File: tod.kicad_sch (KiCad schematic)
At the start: 65 parts, among them J1 2xMVE252, J2 MV133, J3 2xMVE252, J4 MV133, Q1 BC856B, Q2 BC817, Q3 BC856B, Q4 BC817, Q5 BC856B, Q6 BC817, Q7 BC856B, Q8 BC817, U1 PC817, U2 PC817, U3 PC817, U4 PC817

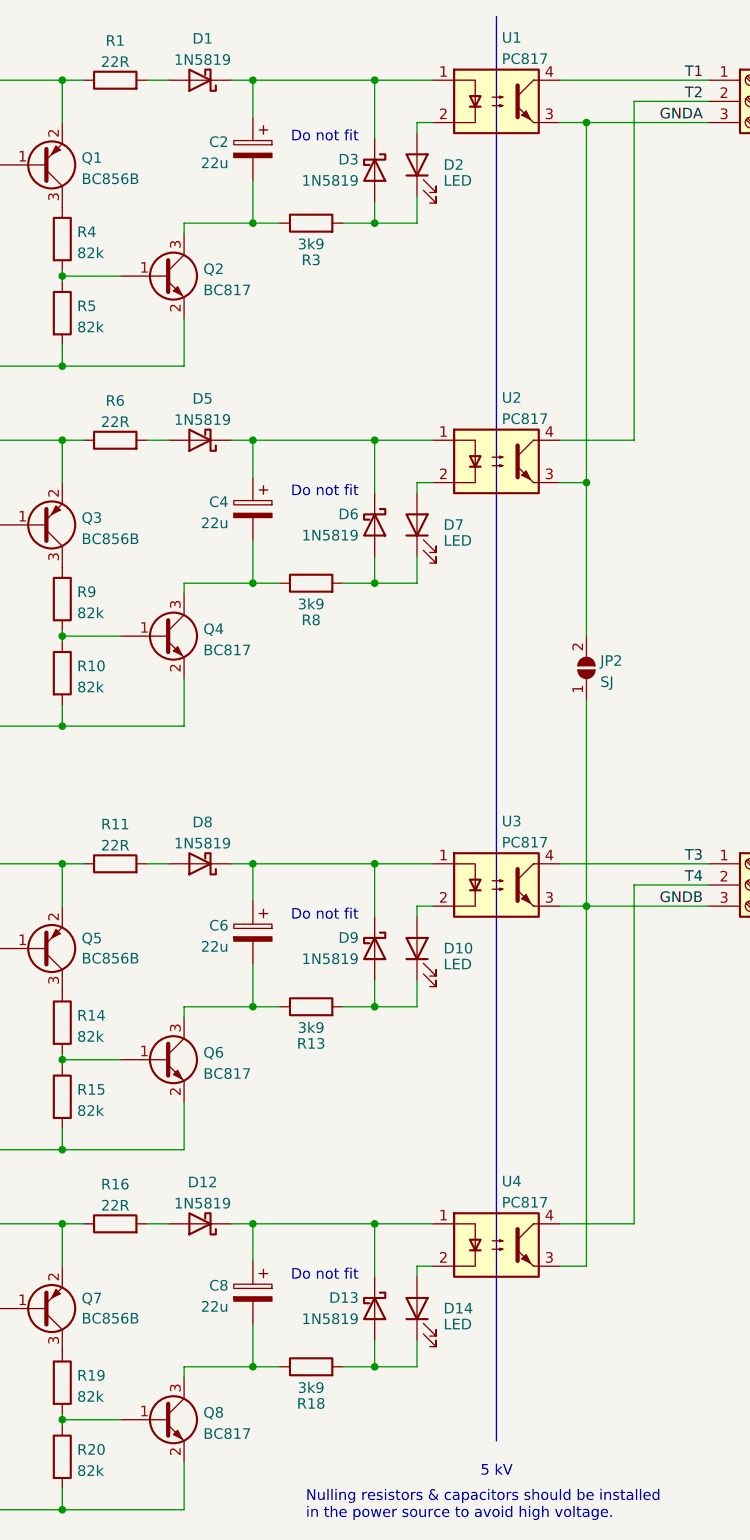
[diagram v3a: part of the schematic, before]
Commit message: Use DNP where appropriate.
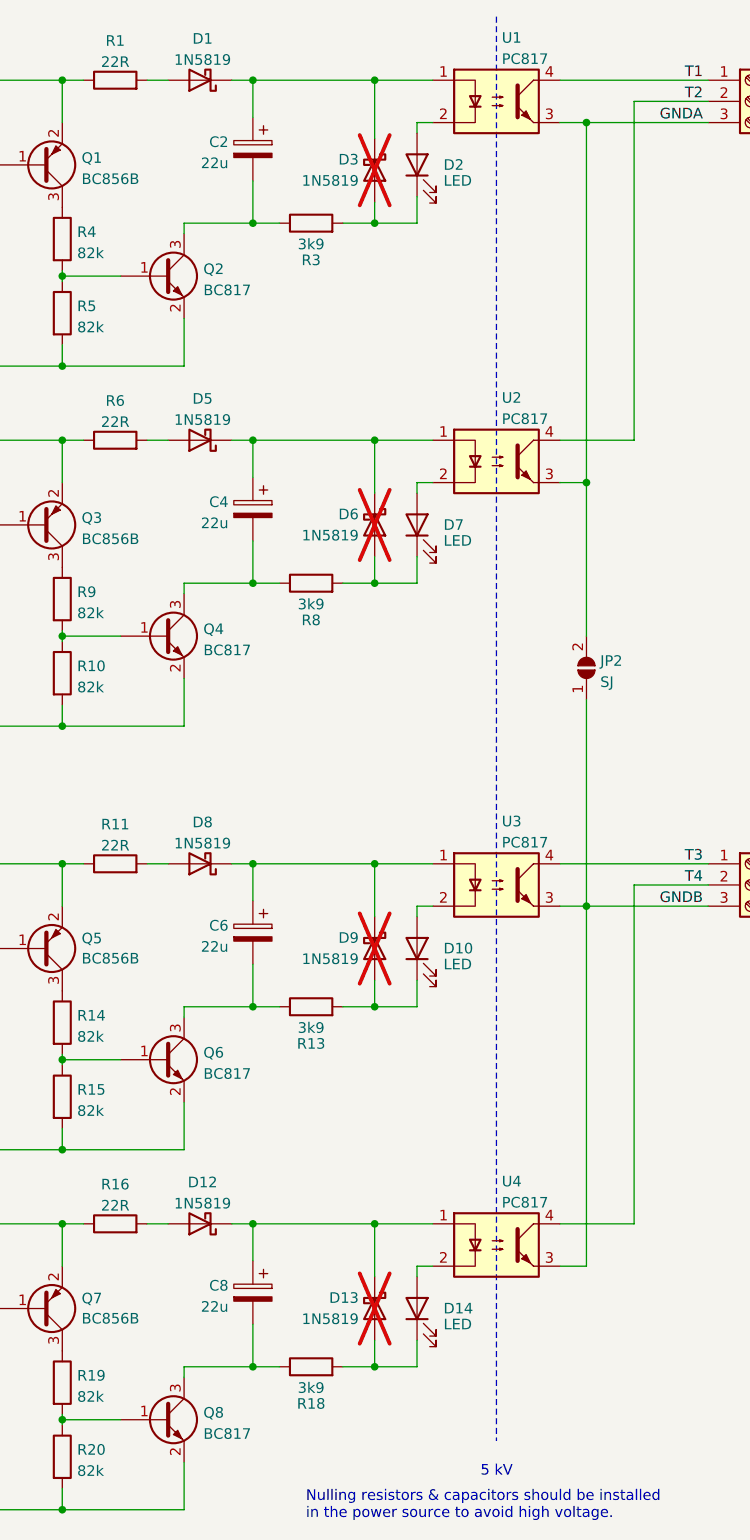
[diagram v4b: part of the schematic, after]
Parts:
- D13, D3, D6, D9: now not fitted
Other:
- note removed: "Do not fit"
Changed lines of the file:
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@@
   )
   (polyline (pts (xy 146.05 13.97) (xy 146.05 184.785))
-    (stroke (width 0) (type default))
+    (stroke (width 0) (type dash))
   )
   (wire (pts (xy 153.67 163.83) (xy 156.845 163.83))
@@
   (wire (pts (xy 131.445 158.75) (xy 138.43 158.75))
     (stroke (width 0) (type default))
-  )
-  (text "Do not fit" (at 129.54 165.735 0)
-    (effects (font (size 1.27 1.27)) (justify right bottom))
-  )
-  (text "Do not fit" (at 129.54 71.755 0)
-    (effects (font (size 1.27 1.27)) (justify right bottom))
   )
   (text "Up to ~2.5 W\nheat loss!" (at 31.242 43.688 0)
@@
     (effects (font (size 1.27 1.27)) (justify left bottom))
   )
-  (text "Do not fit" (at 129.54 122.555 0)
-    (effects (font (size 1.27 1.27)) (justify right bottom))
-  )
-  (text "Do not fit" (at 129.54 29.21 0)
-    (effects (font (size 1.27 1.27)) (justify right bottom))
-  )
   (label "K1" (at 29.21 26.67 0) (fields_autoplaced)
     (effects (font (size 1.27 1.27)) (justify left bottom))
@@
   )
   (symbol (lib_id "Diode:1N5819") (at 131.445 125.73 270) (unit 1)
-    (in_bom yes) (on_board yes) (dnp no)
+    (in_bom yes) (on_board yes) (dnp yes)
     (property "Reference" "D9" (at 129.54 124.46 90)
       (effects (font (size 1.27 1.27)) (justify right))
@@
   )
   (symbol (lib_id "Diode:1N5819") (at 131.445 74.93 270) (unit 1)
-    (in_bom yes) (on_board yes) (dnp no)
+    (in_bom yes) (on_board yes) (dnp yes)
     (property "Reference" "D6" (at 129.54 73.66 90)
       (effects (font (size 1.27 1.27)) (justify right))
@@
   )
   (symbol (lib_id "Diode:1N5819") (at 131.445 32.385 270) (unit 1)
-    (in_bom yes) (on_board yes) (dnp no)
+    (in_bom yes) (on_board yes) (dnp yes)
     (property "Reference" "D3" (at 129.54 31.115 90)
       (effects (font (size 1.27 1.27)) (justify right))
@@
   )
   (symbol (lib_id "Diode:1N5819") (at 131.445 168.91 270) (unit 1)
-    (in_bom yes) (on_board yes) (dnp no)
+    (in_bom yes) (on_board yes) (dnp yes)
     (property "Reference" "D13" (at 129.54 167.64 90)
       (effects (font (size 1.27 1.27)) (justify right))

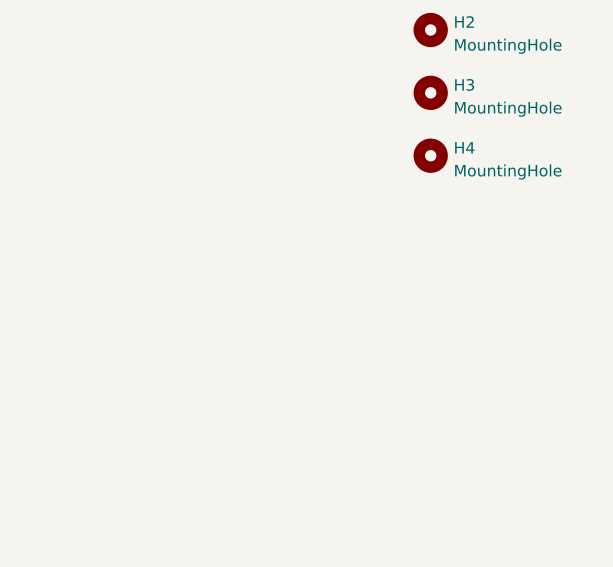
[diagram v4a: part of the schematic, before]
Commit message: Add note regarding LEDs brightness.
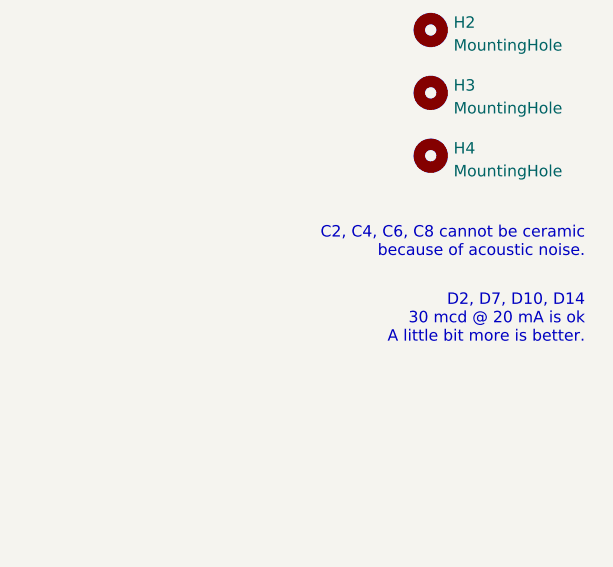
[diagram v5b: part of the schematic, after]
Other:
- note added: "C2, C4, C6, C8 cannot be ceramic because of acoustic noise."
- note added: "D2, D7, D10, D14 30 mcd @ 20 mA is ok A little bit more is better."
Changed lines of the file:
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@@
     (effects (font (size 1.27 1.27)) (justify left bottom))
+  )
+  (text "D2, D7, D10, D14\n30 mcd @ 20 mA is ok\nA little bit more is better."
+    (at 280.035 62.23 0)
+    (effects (font (size 1.27 1.27)) (justify right bottom))
+  )
+  (text "C2, C4, C6, C8 cannot be ceramic\nbecause of acoustic noise."
+    (at 280.035 52.705 0)
+    (effects (font (size 1.27 1.27)) (justify right bottom))
   )
   (label "K1" (at 29.21 26.67 0) (fields_autoplaced)

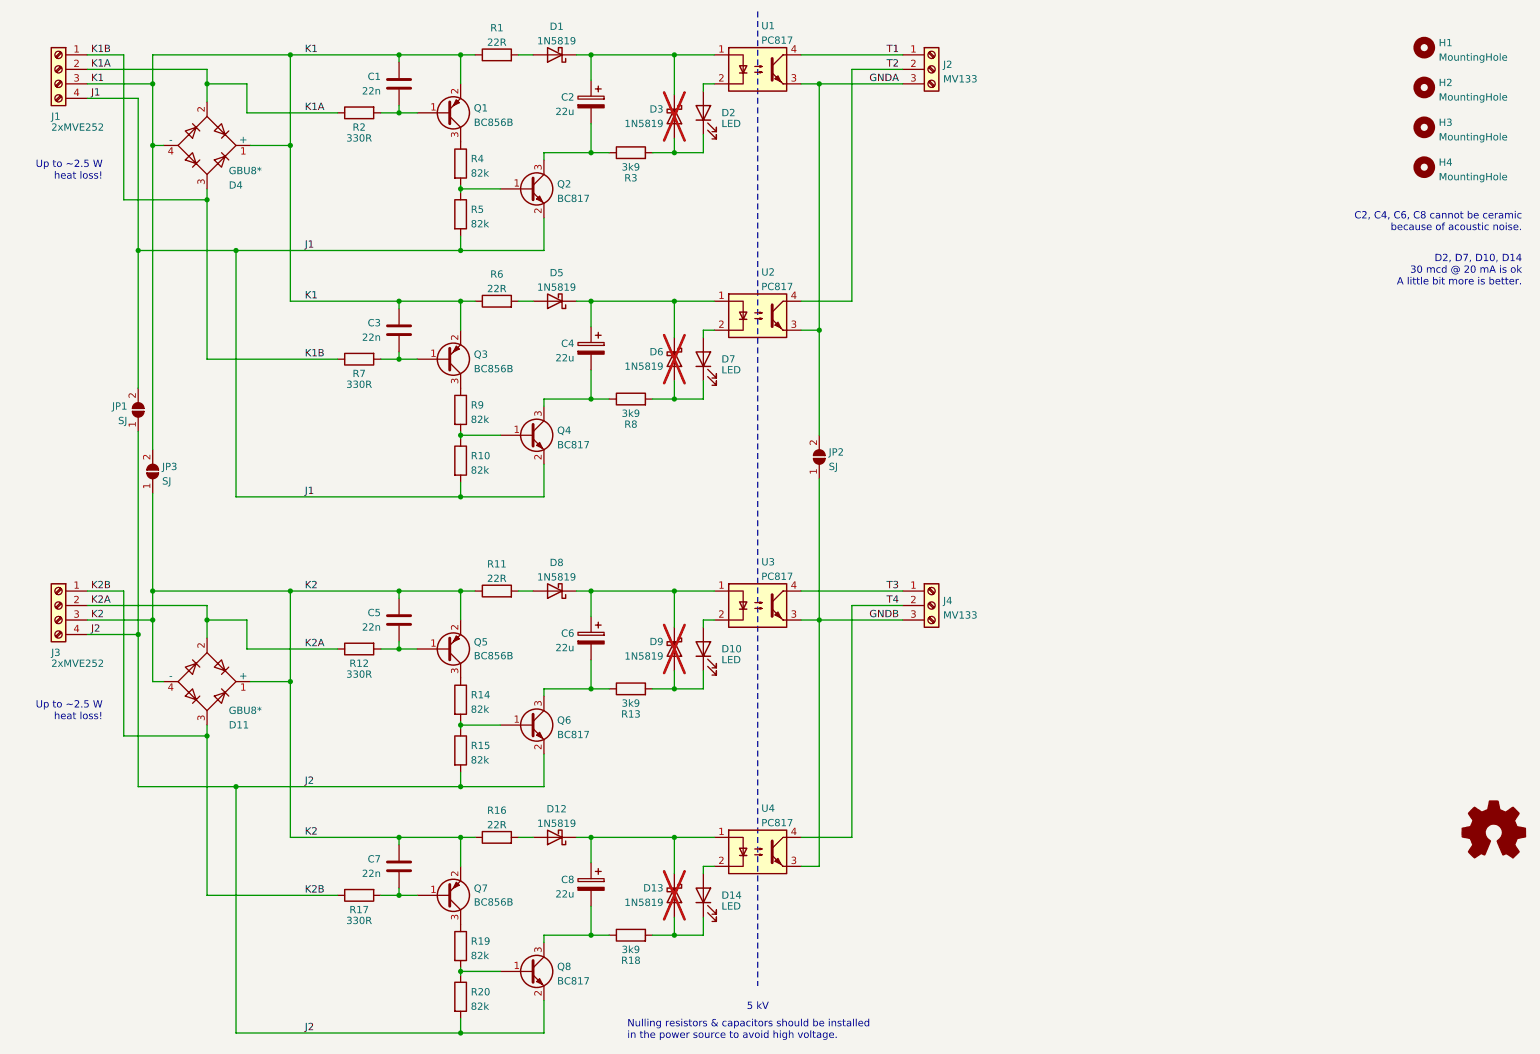
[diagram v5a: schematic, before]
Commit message: 22n -> 10n damping capacitors.
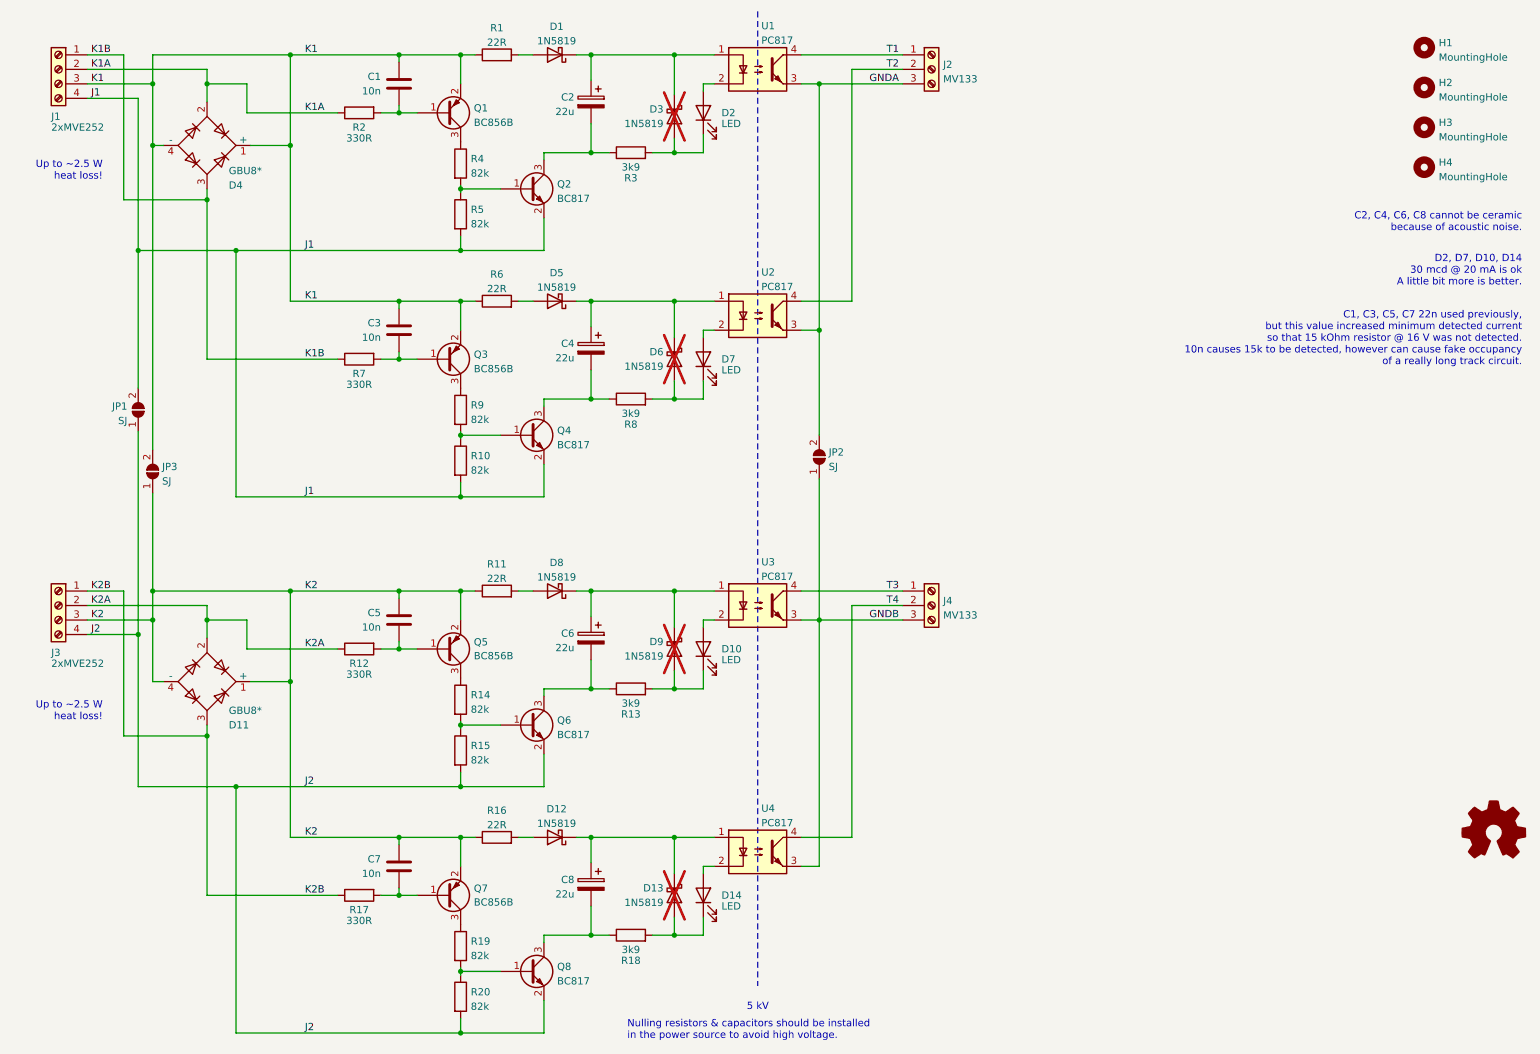
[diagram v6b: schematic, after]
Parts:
- C1, C3, C5, C7: value 22n -> 10n; LCSC C1729 -> C1710
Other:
- note added: "C1, C3, C5, C7 22n used previously, but this value increased minimum detected current so that 15 kOhm resistor @ 16 V was not detected. 10n causes 15k to be detected, however can cause fake occupancy of a really long track circuit."
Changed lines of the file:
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@@
   (title_block
     (title "DCC Track Occupancy Detector")
-    (date "2023-04-20")
-    (rev "1.3")
+    (date "2024-02-22")
+    (rev "1.4")
     (company "Model Railroader Club Brno I – KMŽ Brno I – https://kmz-brno.cz/")
     (comment 1 "Jan Horáček")
@@
     (stroke (width 0) (type default))
   )
+  (text "C1, C3, C5, C7 22n used previously,\nbut this value increased minimum detected current\nso that 15 kOhm resistor @ 16 V was not detected.\n10n causes 15k to be detected, however can cause fake occupancy\nof a really long track circuit."
+    (at 280.035 76.2 0)
+    (effects (font (size 1.27 1.27)) (justify right bottom))
+  )
   (text "Up to ~2.5 W\nheat loss!" (at 31.242 43.688 0)
     (effects (font (size 1.27 1.27)) (justify right bottom))
@@
       (effects (font (size 1.27 1.27)) (justify right))
     )
-    (property "Value" "22n" (at 80.01 121.92 0)
+    (property "Value" "10n" (at 80.01 121.92 0)
       (effects (font (size 1.27 1.27)) (justify right))
     )
@@
       (effects (font (size 1.27 1.27)) hide)
     )
-    (property "LCSC" "C1729" (at 83.185 120.65 0)
+    (property "LCSC" "C1710" (at 83.185 120.65 0)
       (effects (font (size 1.27 1.27)) hide)
     )
@@
       (effects (font (size 1.27 1.27)) (justify right))
     )
-    (property "Value" "22n" (at 80.01 27.94 0)
+    (property "Value" "10n" (at 80.01 27.94 0)
       (effects (font (size 1.27 1.27)) (justify right))
     )
@@
       (effects (font (size 1.27 1.27)) hide)
     )
-    (property "LCSC" "C1729" (at 83.185 26.67 0)
+    (property "LCSC" "C1710" (at 83.185 26.67 0)
       (effects (font (size 1.27 1.27)) hide)
     )
@@
       (effects (font (size 1.27 1.27)) (justify right))
     )
-    (property "Value" "22n" (at 80.01 71.12 0)
+    (property "Value" "10n" (at 80.01 71.12 0)
       (effects (font (size 1.27 1.27)) (justify right))
     )
@@
       (effects (font (size 1.27 1.27)) hide)
     )
-    (property "LCSC" "C1729" (at 83.185 69.85 0)
+    (property "LCSC" "C1710" (at 83.185 69.85 0)
       (effects (font (size 1.27 1.27)) hide)
     )
@@
       (effects (font (size 1.27 1.27)) (justify right))
     )
-    (property "Value" "22n" (at 80.01 165.1 0)
+    (property "Value" "10n" (at 80.01 165.1 0)
       (effects (font (size 1.27 1.27)) (justify right))
     )
@@
       (effects (font (size 1.27 1.27)) hide)
     )
-    (property "LCSC" "C1729" (at 83.185 163.83 0)
-      (effects (font (size 1.27 1.27)) hide)
-    )
+    (property "LCSC" "C1710" (at 83.185 163.83 0)
+      (effects (font (size 1.27 1.27)) hide)
+    )
